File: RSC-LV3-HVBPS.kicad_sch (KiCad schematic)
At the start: 18 parts, among them J17 Molex 43045-0400, J18 Molex 43045-0400, J19 Molex 43045-0400, Q11 AO3400A, Q12 AO3400A

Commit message: initial layout
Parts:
- added J20: Molex 43045-0400, Connector_Molex:Molex_Micro-Fit_3.0_43045-0412_2x02_P3.00mm_Vertical, symbol Connector_Generic:Conn_02x02_Top_Bottom
- added J6, J7: Conn_01x04, Connector_Molex:Molex_KK-254_AE-6410-04A_1x04_P2.54mm_Vertical, symbol Connector_Generic:Conn_01x04
- added R70, R71: 5.1k, Resistor_SMD:R_0603_1608Metric_Pad0.98x0.95mm_HandSolder, symbol Device:R
- J17, J18, J19: footprint Project_Library:Molex_Micro-Fit_3.0_43045-0400_2x02_P3.00mm_Horizontal_VerticalCompatible -> Connector_Molex:Molex_Micro-Fit_3.0_43045-0412_2x02_P3.00mm_Vertical
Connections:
- net +12V: now also J6.2 (Pin_2), J7.2 (Pin_2)
- net GND: now also J6.1 (Pin_1), J7.1 (Pin_1)
- net at D44.1 (K), J17.3 (Pin_3), J18.2 (Pin_2)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: now also J20.3 (Pin_3)
- net at D44.2 (A), J17.4 (Pin_4), Q11.3 (D): now also J20.4 (Pin_4)
- new net +3.3V: R70.1, R71.1
- new net FAN_1_PWM: J6.4 (Pin_4)
- new net FAN_1_TACH: J6.3 (Pin_3), R70.2
- new net FAN_2_PWM: J7.4 (Pin_4)
- new net FAN_2_TACH: J7.3 (Pin_3), R71.2
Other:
- moved on the sheet: C39, D46, J19, R68, R69

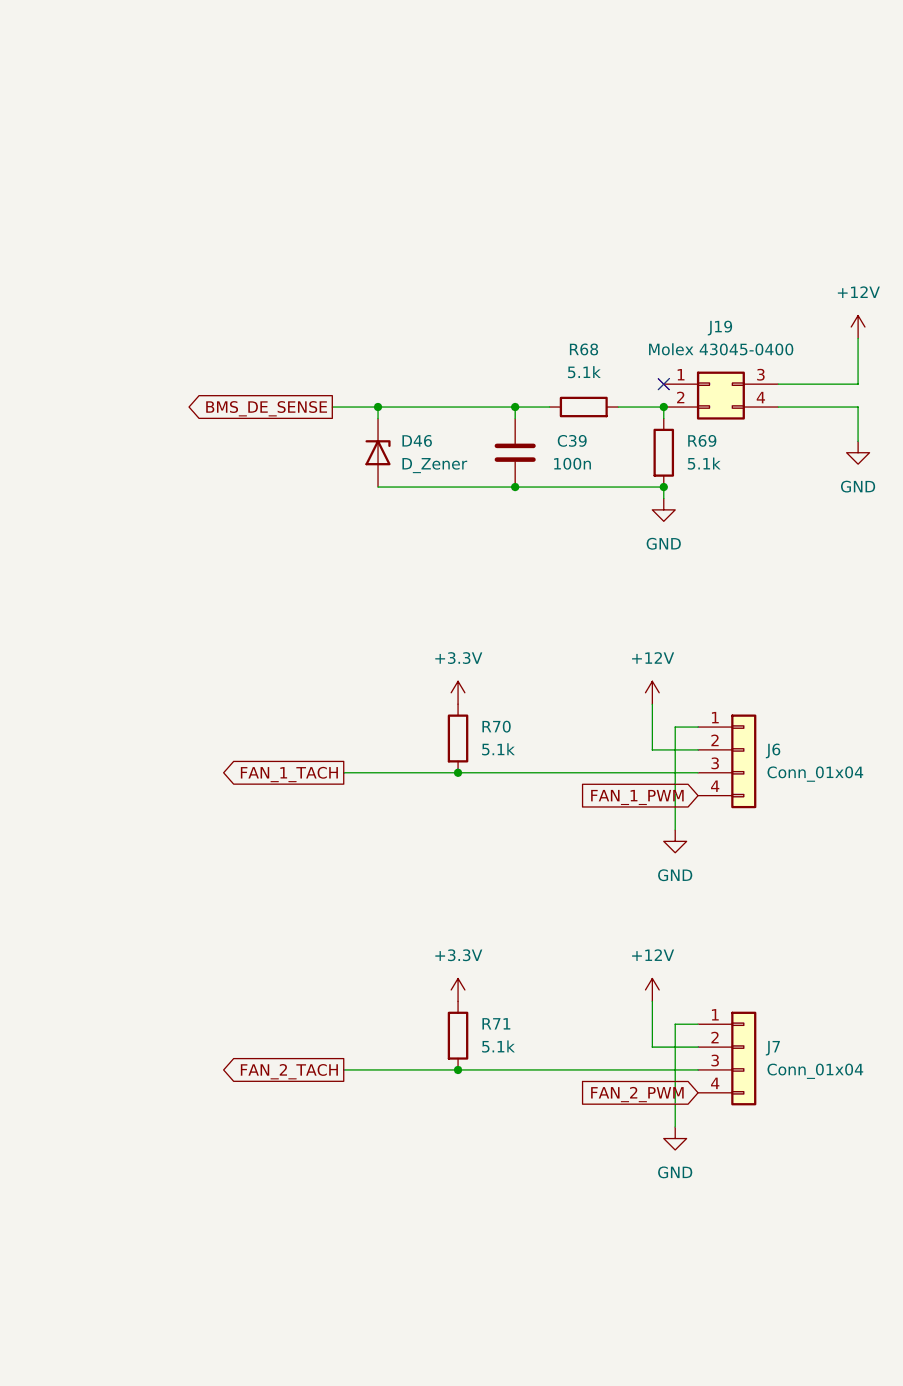
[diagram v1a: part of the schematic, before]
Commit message: more layout and some initial routing
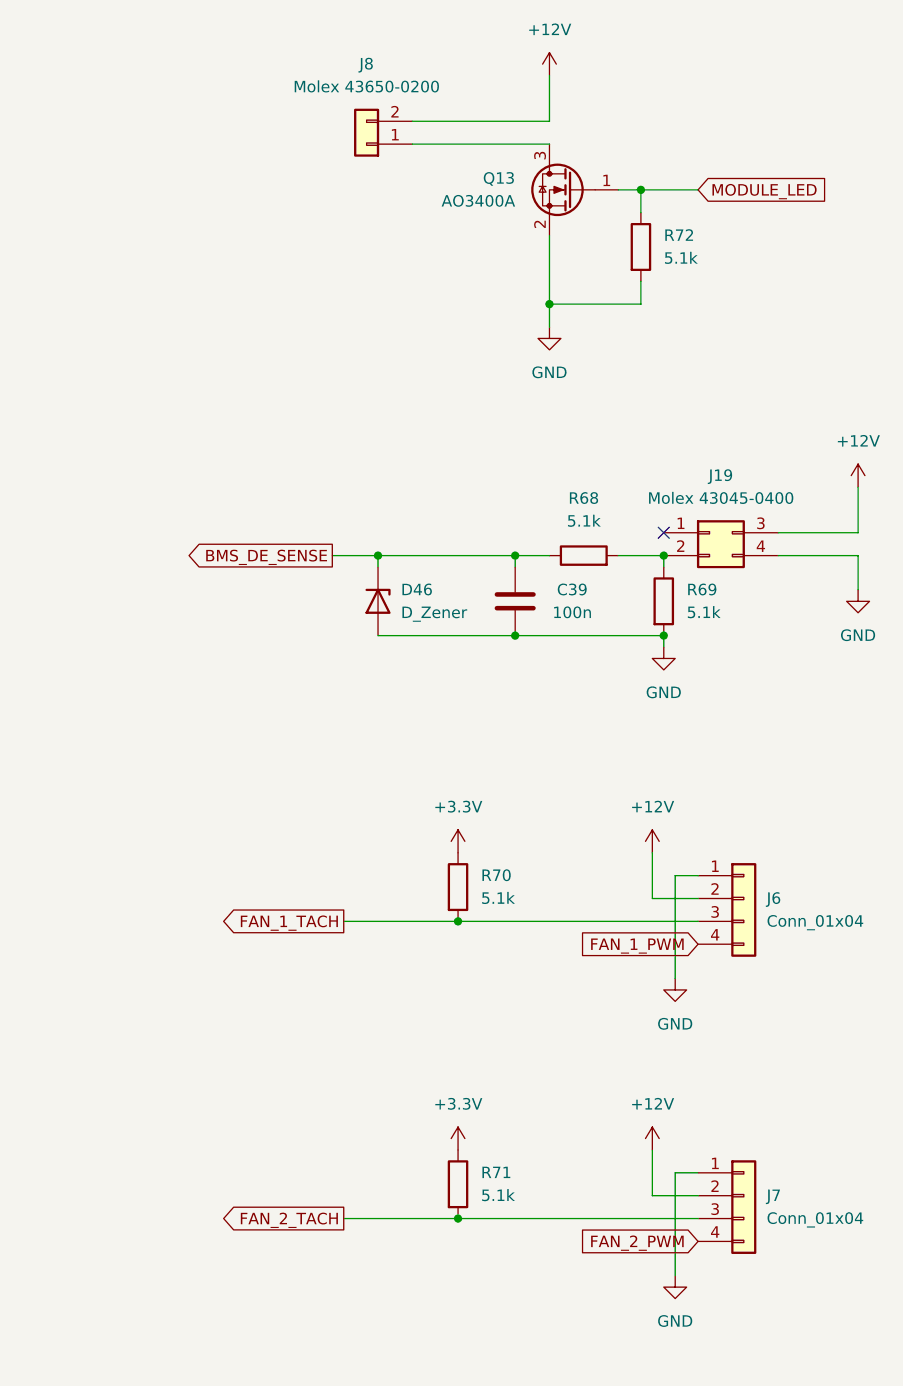
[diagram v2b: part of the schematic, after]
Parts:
- added J8: Molex 43650-0200, Connector_Molex:Molex_Micro-Fit_3.0_43650-0215_1x02_P3.00mm_Vertical, symbol Connector_Generic:Conn_01x02
- added Q13: AO3400A, Package_TO_SOT_SMD:SOT-23, symbol Transistor_FET:AO3400A
- added R72: 5.1k, Resistor_SMD:R_0603_1608Metric_Pad0.98x0.95mm_HandSolder, symbol Device:R
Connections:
- net +12V: now also J8.2 (Pin_2)
- net GND: now also Q13.2 (S), R72.2
- new net: J8.1 (Pin_1), Q13.3 (D)
- new net MODULE_LED: Q13.1 (G), R72.1
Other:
- moved on the sheet: C39, D46, J19, J6, J7, R68, R69, R70, R71

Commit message: r0 final
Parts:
- renumbered C38 to C1, C39 to C2, D43 to D1, D44 to D2, D45 to D3, D46 to D4, J20 to J1, J17 to J2, J18 to J3, J8 to J4, J19 to J5, Q11 to Q1, Q12 to Q2, Q13 to Q3, R63 to R1, R69 to R10, R64 to R2, R65 to R3, R66 to R4, R67 to R5, R70 to R6, R71 to R7, R68 to R8, R72 to R9
